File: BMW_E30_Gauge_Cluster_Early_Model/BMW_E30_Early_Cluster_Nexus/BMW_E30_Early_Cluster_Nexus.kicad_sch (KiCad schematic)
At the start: 27 parts, among them J1 C1 - Blue Connector, J2 C2 - White Connector, J3 C3 - Yellow Connector, J4 Conn_01x16_Pin, J5 Conn_01x19_Socket, U1 Temperature Gauge, U2 Fuel Gauge

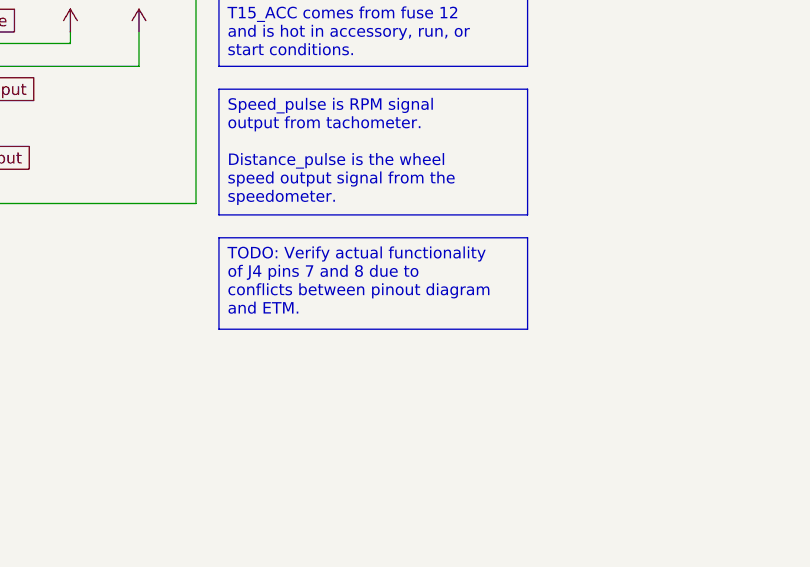
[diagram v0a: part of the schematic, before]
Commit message: Started Tach and EG Schematics
Started pinouts for tachometer and EG schematics. Also made a notation update to the Nexus schematic, removed a TODO that was completed.
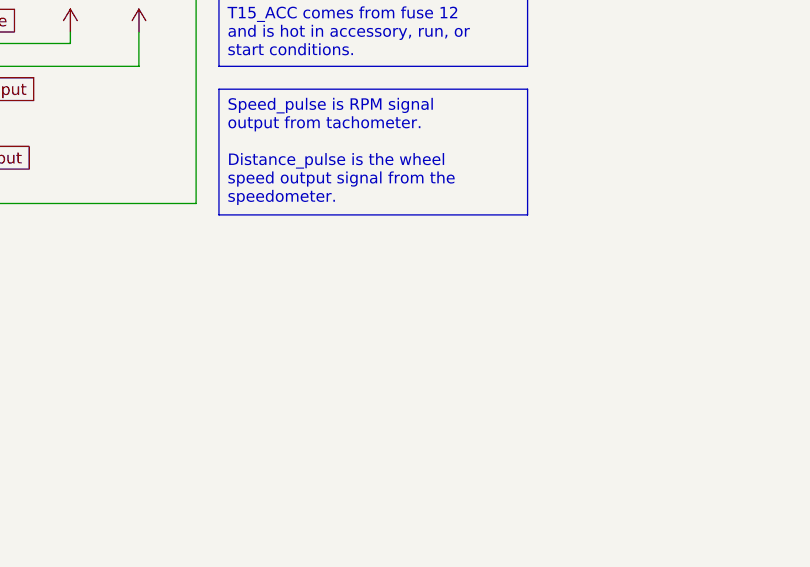
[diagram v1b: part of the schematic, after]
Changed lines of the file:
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@@
-		)
-	)
-	(text_box "TODO: Verify actual functionality of J4 pins 7 and 8 due to conflicts between pinout diagram and ETM. "
-		(exclude_from_sim no)
-		(at 151.13 140.97 0)
-		(size 34.29 10.16)
-		(margins 0.9525 0.9525 0.9525 0.9525)
-		(stroke
-			(width 0)
-			(type solid)
-		)
-		(fill
-			(type color)
-			(color 255 255 0 1)
-		)
-		(effects
-			(font
-				(size 1.27 1.27)
-			)
-			(justify left top)
 		)
 	)

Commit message: Add Digikey Part Numbers
Added digikey part numbers for resistors and connectors for ordering purposes.
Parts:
- J1: Digikey Part No. (none) -> 827881-3-ND
- J2: Digikey Part No. (none) -> A129100-ND
- J3: Digikey Part No. (none) -> A129099-ND
- R1: Digikey Part No. (none) -> CF14JT16K0CT-ND
- R2, R3: Digikey Part No. (none) -> 2019-PCF1C680K-ND
- R4: Digikey Part No. (none) -> 541-CMF65100R00FKEBCT-ND

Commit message: Nexus Layout Updates + Footprint Updates
Updated fuel gauge and temp gauge footprints to have their locating holes included. Also widened the mounting holes for both gauge footprints.

Layout:
Moved fuel gauge to the right by 1mm, moved blue connector down 1mm and left 0.5mm, moved white connector down 1mm.
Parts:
- U1: footprint BMW_Cluster_Connectors:Gauge_fuel_temp -> BMW_Cluster_Connectors:Gauge_Temp
- U2: footprint BMW_Cluster_Connectors:Gauge_fuel_temp -> BMW_Cluster_Connectors:Gauge_Fuel
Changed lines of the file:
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@@
 			)
 		)
-		(property "Footprint" "BMW_Cluster_Connectors:Gauge_fuel_temp"
+		(property "Footprint" "BMW_Cluster_Connectors:Gauge_Fuel"
 			(at 135.89 210.82 0)
 			(effects
@@
 			)
 		)
-		(property "Footprint" "BMW_Cluster_Connectors:Gauge_fuel_temp"
+		(property "Footprint" "BMW_Cluster_Connectors:Gauge_Temp"
 			(at 213.36 210.82 0)
 			(effects

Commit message: Schematic Readability updates
Changed connector naming to include part numbers for reference purposes. Updated date and version number on schematic, also exported new schematic v3 pdf.
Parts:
- J1: value C1 - Blue Connector -> C1 - Blue Connector (TE_827881-3)
- J2: value C2 - White Connector -> C2 - White Connector (TE_827881-2)
- J3: value C3 - Yellow Connector -> C3 - Yellow Connector (TE_827881-1)
- J4: value Conn_01x16_Pin -> EG_Tach_Spdometer
- J5: value Conn_01x19_Socket -> SI Board Interface
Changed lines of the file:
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@@
 	(title_block
 		(title "BMW E30 Instrument Cluster Nexus")
-		(rev "0")
+		(date "2025-11-10")
+		(rev "3")
 		(company "EGR: Reagan Ansel")
 		(comment 1 "Replacement part for BMW part number: 62111372255")
@@
 		(on_board yes)
 		(dnp no)
-		(fields_autoplaced yes)
 		(property "Reference" "J4"
 			(at 102.235 93.98 0)
@@
 			)
 		)
-		(property "Value" "Conn_01x16_Pin"
-			(at 102.235 96.52 0)
+		(property "Value" "EG_Tach_Spdometer"
+			(at 101.346 96.52 0)
 			(effects
 				(font
@@
 			)
 		)
-		(property "Value" "Conn_01x19_Socket"
+		(property "Value" "SI Board Interface"
 			(at 29.845 96.52 0)
 			(effects
@@
 			)
 		)
-		(property "Value" "C2 - White Connector"
+		(property "Value" "C2 - White Connector (TE_827881-2)"
 			(at 196.85 33.02 0)
 			(effects
@@
 			)
 		)
-		(property "Value" "C1 - Blue Connector"
+		(property "Value" "C1 - Blue Connector (TE_827881-3)"
 			(at 72.39 31.75 0)
 			(effects
@@
 			)
 		)
-		(property "Value" "C3 - Yellow Connector"
+		(property "Value" "C3 - Yellow Connector (TE_827881-1)"
 			(at 323.85 33.02 0)
 			(effects

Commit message: Updated Connector V Footprint
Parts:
- J5: footprint BMW_Cluster_Connectors:ConnectorV_Early -> BMW_Cluster_Connectors:ConnectorV_Early_V2
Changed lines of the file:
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@@
 			)
 		)
-		(property "Footprint" "BMW_Cluster_Connectors:ConnectorV_Early"
+		(property "Footprint" "BMW_Cluster_Connectors:ConnectorV_Early_V2"
 			(at 29.21 121.92 0)
 			(effects

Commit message: Update Schematic PDFs
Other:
- company: EGR: Reagan Ansel -> Reans
